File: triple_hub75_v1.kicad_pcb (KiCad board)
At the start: 2 copper layers, 69.1 x 95 mm, 9 parts, among them J1 Conn_02x08_Odd_Even, J2 Raspberry_Pi_2_3, J3 Conn_01x03, J4 Conn_02x08_Odd_Even, J5 Conn_02x08_Odd_Even, U1 74HC245, U2 74HC245, U3 74HC245, U4 74HC245

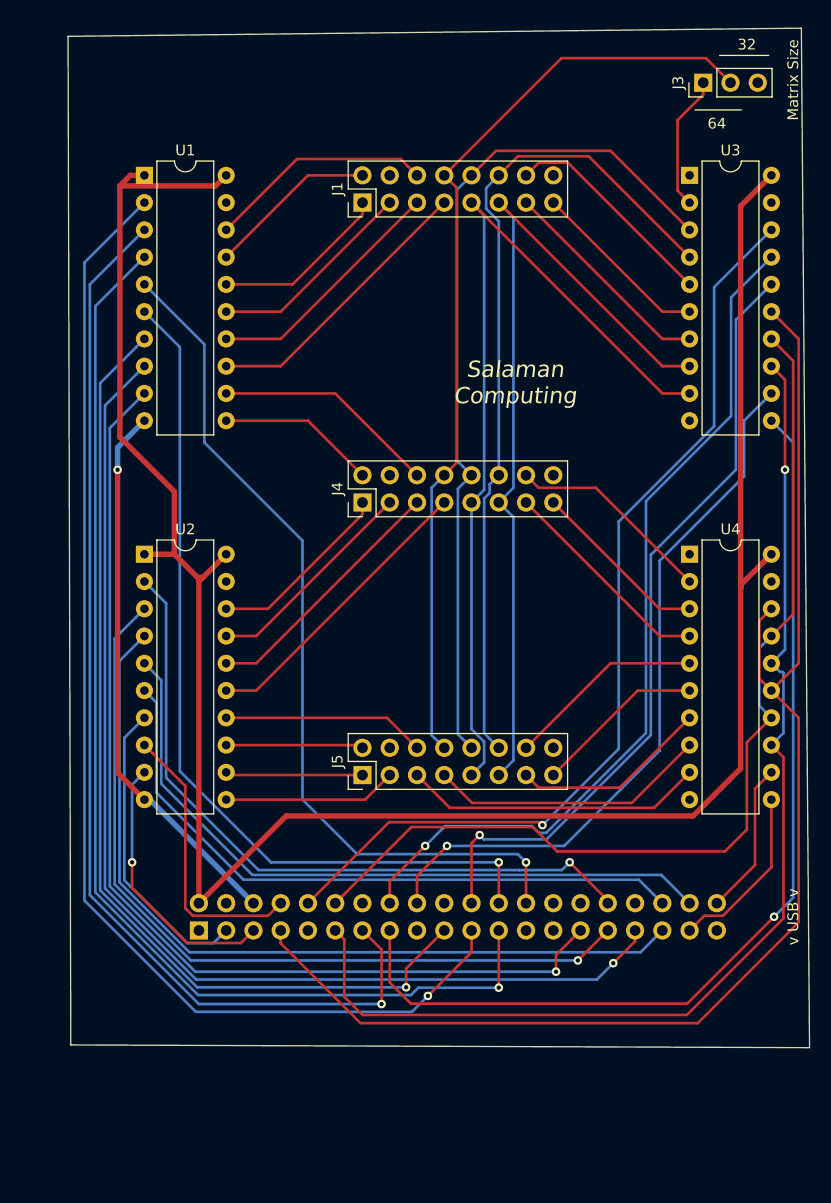
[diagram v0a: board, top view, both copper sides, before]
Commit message: remove left side tracks
Step One:  I want to move the left side traces from the bottom layer to the top so that I can use bottom layer as ground plane.  They'll still be some on bottom, but I want to make the default the top layer.
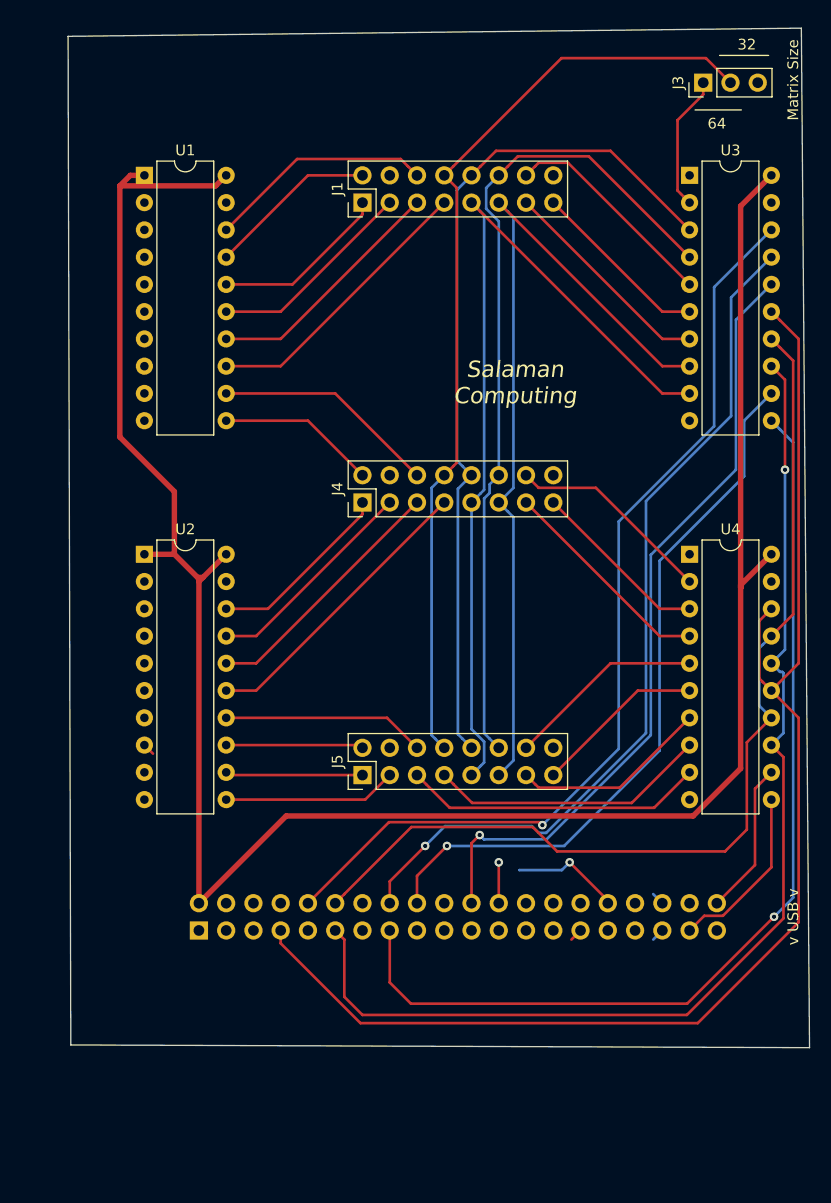
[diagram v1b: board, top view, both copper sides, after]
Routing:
- net /G2_M1_Pi: track 112.0 -> 0.00 mm, vias 1 -> 0
- net /R1_M1_Pi: track 108.5 -> 0.25 mm, vias 1 -> 0
- net /G2_M2_Pi: track 105.6 -> 0.00 mm, vias 1 -> 0
- net /G1_M1_Pi: track 103.1 -> 0.00 mm, vias 1 -> 0
- net /G1_M2_Pi: track 96.9 -> 1.20 mm, vias 1 -> 0
- net /B2_M1_Pi: track 92.1 -> 0.00 mm, vias 1 -> 0
- net /B1_M1_Pi: track 81.2 -> 0.00 mm, vias 1 -> 0
- net /R2_M1_Pi: track 81.2 -> 3.81 mm
- net /B1_M2_Pi: track 76.9 -> 0.00 mm, vias 1 -> 0
- net /R2_M2_Pi: track 78.0 -> 1.20 mm
- net /B2_M2_Pi: track 65.7 -> 0.00 mm
- net /G2_M3_Pi: track 61.4 -> 1.20 mm
- net /R1_M2_Pi: track 65.9 -> 10.2 mm
- net GND: track 52.5 -> 1.52 mm, vias 1 -> 0
- net /G1_M3_Pi: track 28.3 -> 0.00 mm
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
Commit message: U2 re-routed to top
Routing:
- net +5V: track 205.9 -> 59.3 mm
- net /G2_M2_Pi: track 0.00 -> 121.5 mm
- net /G1_M2_Pi: track 1.20 -> 107.1 mm
- net /B1_M2_Pi: track 0.00 -> 87.4 mm, vias 0 -> 1
- net /R2_M2_Pi: track 1.20 -> 87.3 mm, vias 0 -> 1
- net /B2_M2_Pi: track 0.00 -> 85.8 mm
- net /R1_M2_Pi: track 10.2 -> 93.7 mm
- net /G2_M3_Pi: track 1.20 -> 79.7 mm
- net /R1_M3_Pi: track 1.13 -> 36.1 mm
- net /G1_M3_Pi: track 0.00 -> 32.5 mm, vias 0 -> 1
- net /B1_M3_Pi: track 0.00 -> 25.2 mm
- net /STB_Pi: track 125.0 -> 130.1 mm, vias 0 -> 1
- net /R2_M1_Pi: track 3.81 -> 0.00 mm, vias 1 -> 0
- net /A_Pi: track 92.6 -> 94.8 mm, vias 1 -> 2
- net /CLK_Pi: track 106.3 -> 108.3 mm, vias 1 -> 2
- added copper zone on F.Cu, net +5V
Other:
- board size 69.1 x 95 mm -> 69.1 x 106.2 mm

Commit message: Right side routes on F-CU
Ground fill now looks better.  Next step: squeeze in the chips/traces?
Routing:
- net /G2_M1_Pi: track 0.00 -> 134.7 mm, vias 0 -> 1
- net /B1_M1_Pi: track 0.00 -> 131.0 mm, vias 0 -> 1
- net /R1_M1_Pi: track 0.25 -> 128.8 mm, vias 0 -> 1
- net /R2_M1_Pi: track 0.00 -> 124.7 mm, vias 0 -> 1
- net /G1_M1_Pi: track 0.00 -> 122.9 mm, vias 0 -> 1
- net /B2_M1_Pi: track 0.00 -> 109.5 mm, vias 0 -> 1
- net /G1_M2_Pi: track 107.1 -> 112.2 mm, vias 0 -> 1
- net /G2_M2_Pi: track 121.5 -> 122.2 mm, vias 0 -> 1
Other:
- board size 69.1 x 106.2 mm -> 73.4 x 107.4 mm

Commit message: More squeezes
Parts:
- moved U2 5.57 mm to (137.2, 66.3)
- moved U4 5.57 mm to (177.8, 66.3)
- moved U1 5.08 mm to (137.2, 33.3)
- moved U3 5.08 mm to (177.8, 33.3)
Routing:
- net /C_Pi: track 67.6 -> 96.2 mm
- net /A: track 83.0 -> 56.5 mm
- net /C: track 79.7 -> 55.6 mm
- net /B: track 79.8 -> 56.7 mm
- net /D: track 77.9 -> 56.6 mm
- net /CLK_M1: track 20.5 -> 0.00 mm
- net /CLK_M2: track 20.4 -> 0.00 mm
- net /STB_M2: track 19.3 -> 0.00 mm
- net /STB_M1: track 20.4 -> 1.20 mm
- net /STB_Pi: track 130.1 -> 112.4 mm
- net /OE_M1: track 16.9 -> 0.00 mm
- net /OE_M2: track 16.8 -> 0.00 mm
- net /G1_M1_Pi: track 122.9 -> 106.2 mm
- net +5V: track 59.3 -> 73.8 mm
- net /G2_M1_Pi: track 134.7 -> 120.9 mm
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- removed copper zone on F.Cu, net +5V
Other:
- board size 73.4 x 107.4 mm -> 72.6 x 107.4 mm

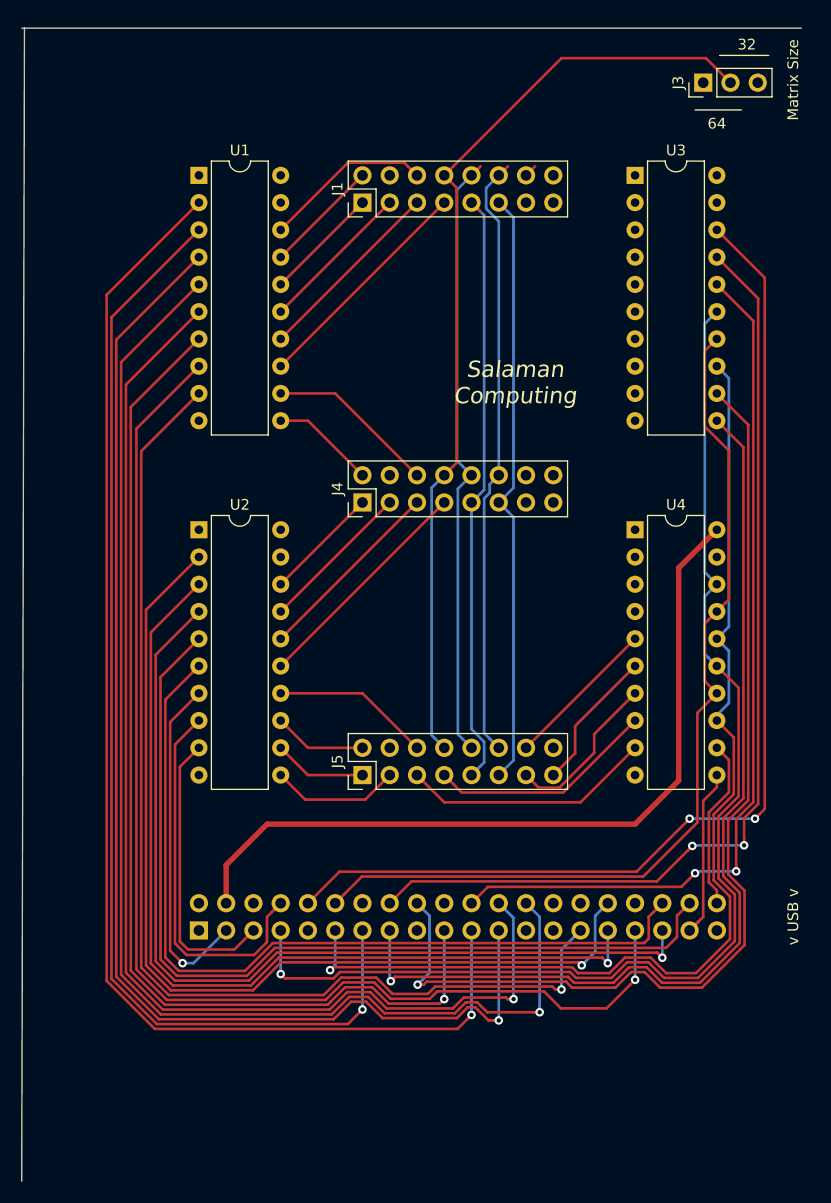
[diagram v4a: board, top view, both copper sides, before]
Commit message: ground plane finished and cleaned
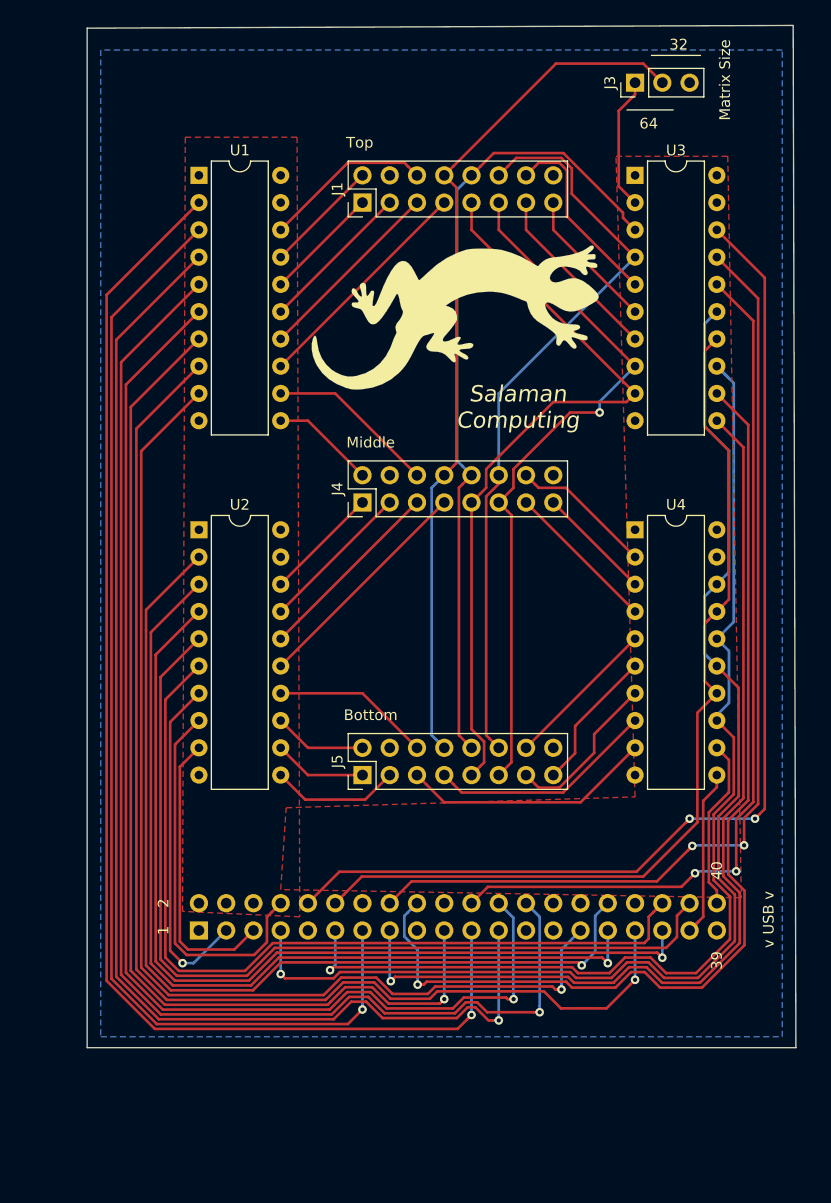
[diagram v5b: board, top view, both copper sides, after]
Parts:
- added G***: LOGO, graphics:salamander_silk_1in, F.Cu at (161.0, 46.5)
- moved J3 6.35 mm to (177.8, 24.6)
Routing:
- net +5V: track 73.8 -> 0.00 mm
- net /B: track 56.7 -> 74.8 mm
- net /CLK_M1: track 0.00 -> 16.9 mm
- net /STB_M1: track 1.20 -> 17.8 mm
- net /A: track 56.5 -> 70.9 mm
- net /CLK_M2: track 0.00 -> 14.4 mm
- net /D: track 56.6 -> 70.5 mm
- net /STB_M2: track 0.00 -> 13.3 mm
- net /OE_M1: track 0.00 -> 13.3 mm
- net /E_Buff: track 0.00 -> 12.4 mm
- net /C: track 55.6 -> 66.4 mm, vias 0 -> 1
- net /OE_M2: track 0.00 -> 10.8 mm
- net /E: track 87.4 -> 80.7 mm
- net /CLK_Pi: track 101.3 -> 103.3 mm
- net /STB_Pi: track 112.4 -> 113.3 mm
- added copper zone on F.Cu, net +5V
- added copper zone on B.Cu, net GND
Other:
- board size 72.6 x 107.4 mm -> 66 x 95.2 mm
- board text added: "1"
- board text added: "2"
- board text added: "39"
- board text added: "40"
- board text added: "Bottom"
- board text added: "Middle"
- board text added: "Top"

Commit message: started silkscreen iupdates
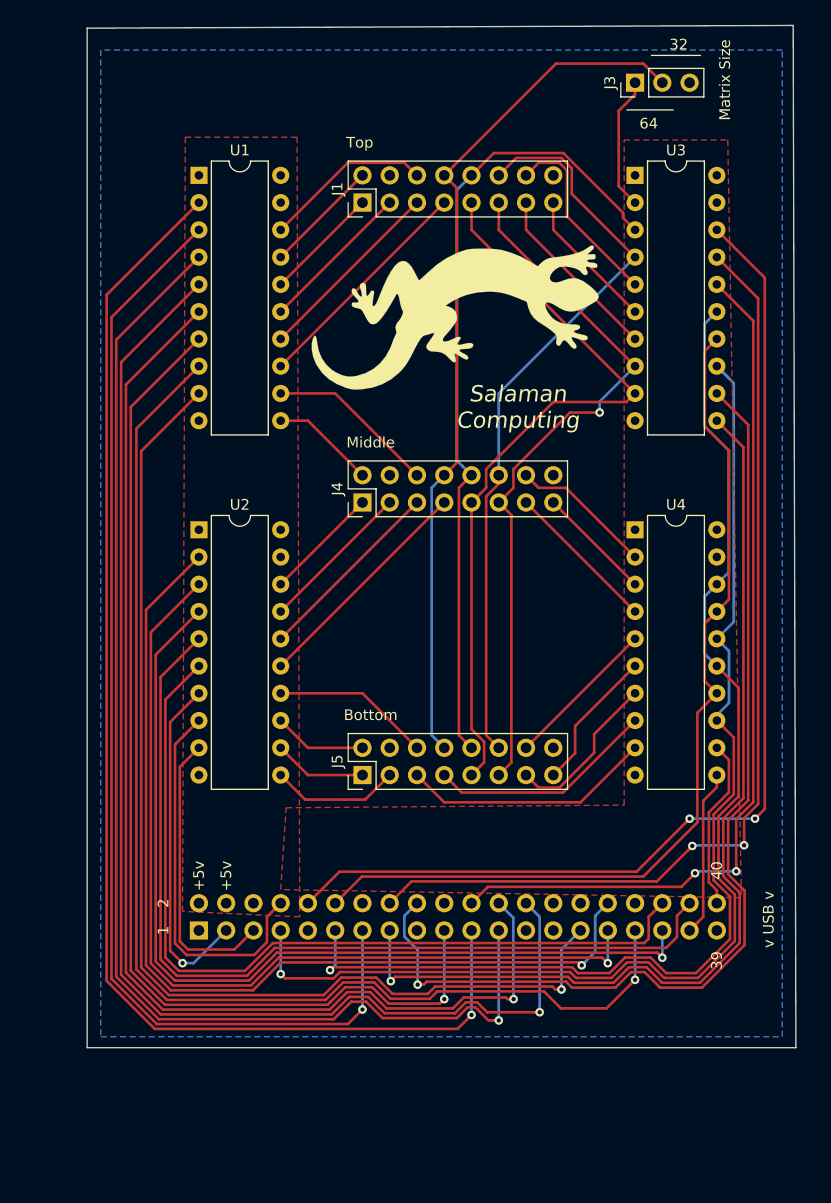
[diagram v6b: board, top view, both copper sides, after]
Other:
- board text added: "+5v"
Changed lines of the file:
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@@
   (general
     (thickness 1.6)
-    (drawings 19)
+    (drawings 21)
     (tracks 485)
     (zones 0)
@@
       (rotate (xyz 0 0 0))
     )
+  )
+  (gr_text +5v (at 139.7 98.552 90) (layer F.SilkS)
+    (effects (font (size 1 1) (thickness 0.15)))
+  )
+  (gr_text +5v (at 137.16 98.552 90) (layer F.SilkS)
+    (effects (font (size 1 1) (thickness 0.15)))
   )
   (gr_text 40 (at 185.42 98.044 90) (layer F.SilkS)
@@
     (polygon
       (pts
-        (xy 176.022 31.496) (xy 186.436 31.496) (xy 187.706 100.584) (xy 144.78 99.822) (xy 145.288 92.202)
-        (xy 177.8 91.186)
+        (xy 176.784 29.972) (xy 186.436 29.972) (xy 187.706 100.584) (xy 144.78 99.822) (xy 145.288 92.202)
+        (xy 176.784 91.948)
       )
     )
